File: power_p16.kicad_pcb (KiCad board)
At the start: 4 copper layers, 44.8 x 41.5 mm, 21 parts, among them J1 LSHM-140-04.0-L-DV-A-N-K-TR, U1 LT8350S

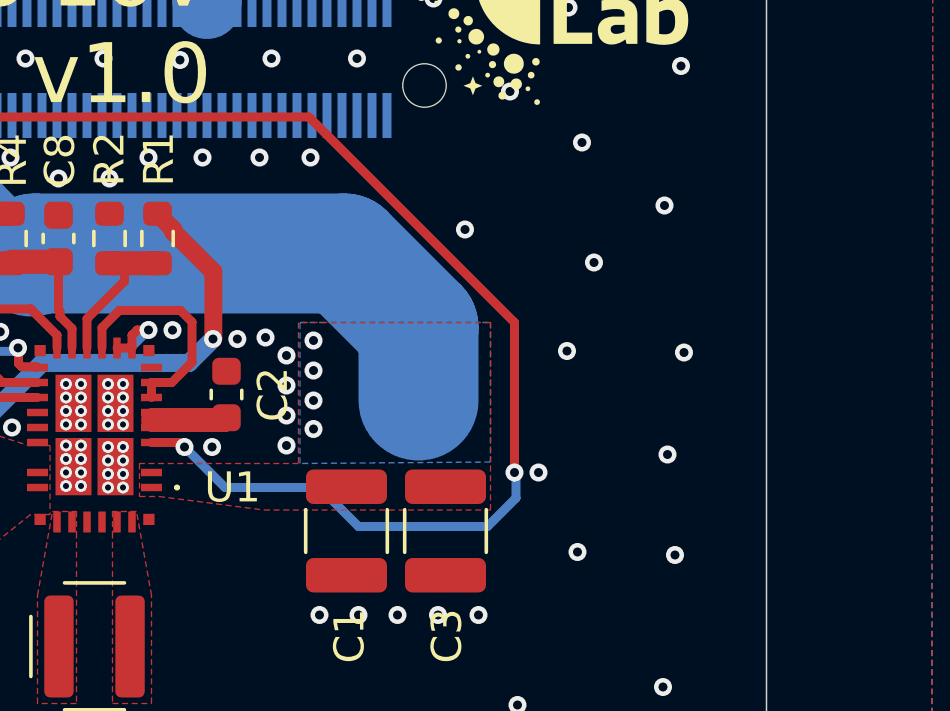
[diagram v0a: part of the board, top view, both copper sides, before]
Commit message: Add input RC snubber
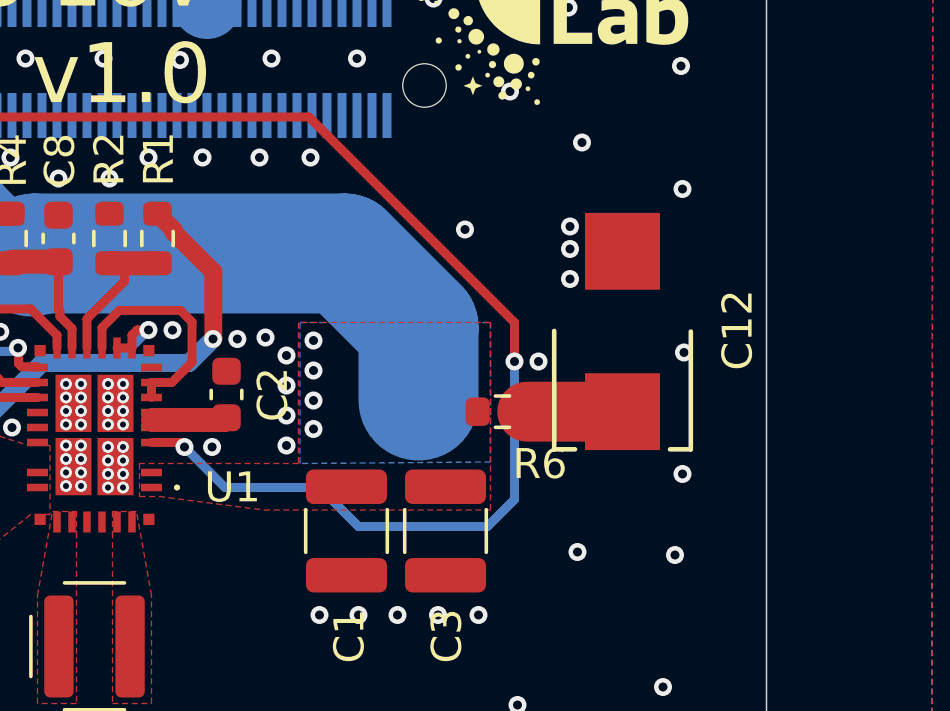
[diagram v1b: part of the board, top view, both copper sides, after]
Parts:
- added C12: 100u, lib:T521X, F.Cu at (64.0, 41.5)
- added R6: 0.5, Resistor_SMD:R_0603_1608Metric, F.Cu at (60.0, 44.2)
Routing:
- net /cf1: track 0.00 -> 3.17 mm
- net GND: vias 155 -> 156
